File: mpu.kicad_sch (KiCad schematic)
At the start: 11 parts, among them IC1 MC6809E, SW1 RESET

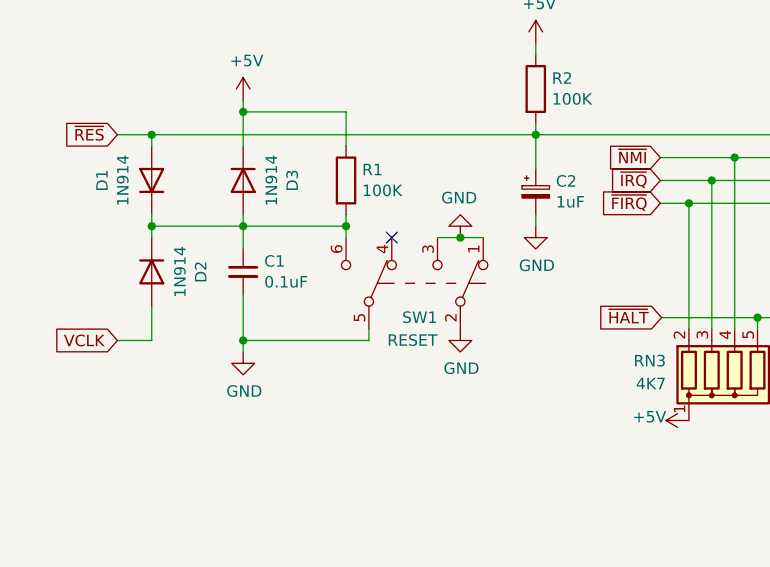
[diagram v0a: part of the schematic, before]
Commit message: rework to flex atx size
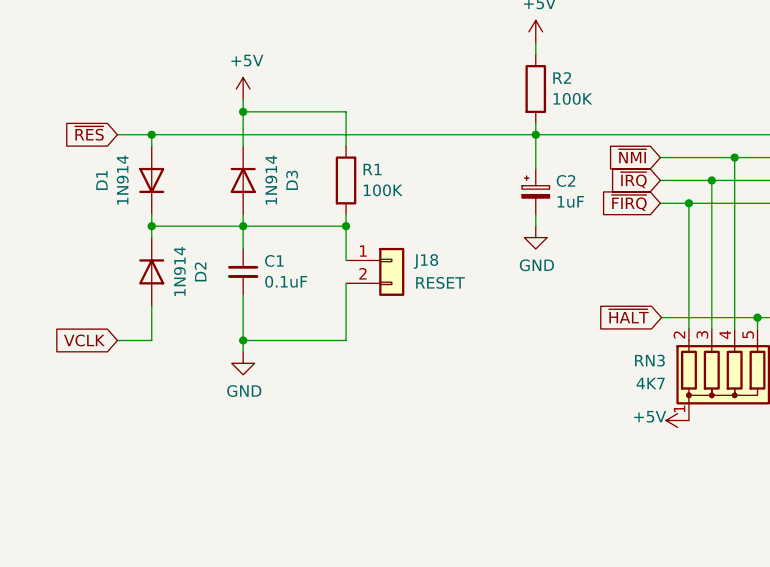
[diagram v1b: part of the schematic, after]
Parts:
- removed SW1: RESET, Dragon:Button_AlpsAlpine_SPUN190900, symbol Switch:SW_Push_DPDT
- added J18: RESET, Connector_PinHeader_2.54mm:PinHeader_1x02_P2.54mm_Vertical, symbol Connector_Generic:Conn_01x02
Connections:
- net GND: now also J18.2 (Pin_2)
- net at C1.1, D1.1 (K), D2.1 (K)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: now also J18.1 (Pin_1)
- no-connect marks 1 -> 0
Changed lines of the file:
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@@
-	)
-	(junction
-		(at 130.81 99.06)
-		(diameter 0)
-		(color 0 0 0 0)
 	)
 	(junction
@@
 		(color 0 0 0 0)
 	)
-	(no_connect
-		(at 123.19 99.06)
-	)
 	(bus_entry
 		(at 166.37 74.93)
@@
 	(wire
 		(pts
-			(xy 120.65 109.22) (xy 120.65 110.49)
-		)
-		(stroke
-			(width 0)
-			(type default)
-		)
-	)
-	(wire
-		(pts
 			(xy 96.52 97.79) (xy 96.52 99.06)
 		)
@@
 		)
 	)
-	(wire
-		(pts
-			(xy 130.81 99.06) (xy 133.35 99.06)
-		)
-		(stroke
-			(width 0)
-			(type default)
-		)
-	)
 	(bus
 		(pts
@@
 	(wire
 		(pts
-			(xy 128.27 99.06) (xy 130.81 99.06)
-		)
-		(stroke
-			(width 0)
-			(type default)
-		)
-	)
-	(wire
-		(pts
 			(xy 139.192 87.63) (xy 139.192 91.44)
 		)
@@
 	(wire
 		(pts
+			(xy 118.11 104.14) (xy 118.11 110.49)
+		)
+		(stroke
+			(width 0)
+			(type default)
+		)
+	)
+	(wire
+		(pts
 			(xy 200.66 64.77) (xy 196.85 64.77)
 		)
@@
 	(wire
 		(pts
+			(xy 118.11 110.49) (xy 106.68 110.49)
+		)
+		(stroke
+			(width 0)
+			(type default)
+		)
+	)
+	(wire
+		(pts
 			(xy 156.21 95.25) (xy 171.45 95.25)
 		)
@@
 	(wire
 		(pts
-			(xy 118.11 97.79) (xy 118.11 99.06)
-		)
-		(stroke
-			(width 0)
-			(type default)
-		)
-	)
-	(wire
-		(pts
 			(xy 200.66 77.47) (xy 196.85 77.47)
 		)
@@
 		)
 	)
+	(wire
+		(pts
+			(xy 118.11 97.79) (xy 118.11 101.6)
+		)
+		(stroke
+			(width 0)
+			(type default)
+		)
+	)
 	(bus
 		(pts
@@
 		(pts
 			(xy 203.2 64.77) (xy 203.2 62.23)
-		)
-		(stroke
-			(width 0)
-			(type default)
-		)
-	)
-	(wire
-		(pts
-			(xy 120.65 110.49) (xy 106.68 110.49)
 		)
 		(stroke
@@
 			)
 			(justify left)
-		)
-	)
-	(symbol
-		(lib_id "power:GND")
-		(at 130.81 99.06 180)
-		(unit 1)
-		(exclude_from_sim no)
-		(in_bom yes)
-		(on_board yes)
-		(dnp no)
-		(property "Reference" "#PWR0135"
-			(at 130.81 92.71 0)
-			(effects
-				(font
-					(size 1.27 1.27)
-				)
-				(hide yes)
-			)
-		)
-		(property "Value" "GND"
-			(at 130.683 94.6658 0)
-			(effects
-				(font
-					(size 1.27 1.27)
-				)
-			)
-		)
-		(property "Footprint" ""
-			(at 130.81 99.06 0)
-			(effects
-				(font
-					(size 1.27 1.27)
-				)
-				(hide yes)
-			)
-		)
-		(property "Datasheet" ""
-			(at 130.81 99.06 0)
-			(effects
-				(font
-					(size 1.27 1.27)
-				)
-				(hide yes)
-			)
-		)
-		(property "Description" ""
-			(at 130.81 99.06 0)
-			(effects
-				(font
-					(size 1.27 1.27)
-				)
-				(hide yes)
-			)
-		)
-		(pin "1"
-		)
-		(instances
-			(project "DragonRevX4Plus"
-				(path "/280624a6-9139-42c2-8c41-e9b53b8715d2/dfedbe1d-4fb5-427e-80c5-e29061a6defc"
-					(reference "#PWR0135")
-					(unit 1)
-				)
-			)
 		)
 	)
@@
 	)
 	(symbol
-		(lib_id "power:GND")
-		(at 130.81 109.22 0)
-		(unit 1)
-		(exclude_from_sim no)
-		(in_bom yes)
-		(on_board yes)
-		(dnp no)
-		(property "Reference" "#PWR064"
-			(at 130.81 115.57 0)
-			(effects
-				(font
-					(size 1.27 1.27)
-				)
-				(hide yes)
-			)
-		)
-		(property "Value" "GND"
-			(at 130.937 113.6142 0)
-			(effects
-				(font
-					(size 1.27 1.27)
-				)
-			)
-		)
-		(property "Footprint" ""
-			(at 130.81 109.22 0)
-			(effects
-				(font
-					(size 1.27 1.27)
-				)
-				(hide yes)
-			)
-		)
-		(property "Datasheet" ""
-			(at 130.81 109.22 0)
-			(effects
-				(font
-					(size 1.27 1.27)
-				)
-				(hide yes)
-			)
-		)
-		(property "Description" ""
-			(at 130.81 109.22 0)
-			(effects
-				(font
-					(size 1.27 1.27)
-				)
-				(hide yes)
-			)
-		)
-		(pin "1"
-		)
-		(instances
-			(project "DragonRevX4Plus"
-				(path "/280624a6-9139-42c2-8c41-e9b53b8715d2/dfedbe1d-4fb5-427e-80c5-e29061a6defc"
-					(reference "#PWR064")
-					(unit 1)
-				)
-			)
-		)
-	)
-	(symbol
 		(lib_id "Diode:1N914")
 		(at 106.68 92.71 270)
@@
 				(path "/280624a6-9139-42c2-8c41-e9b53b8715d2/dfedbe1d-4fb5-427e-80c5-e29061a6defc"
 					(reference "#PWR06")
+					(unit 1)
+				)
+			)
+		)
+	)
+	(symbol
+		(lib_id "Connector_Generic:Conn_01x02")
+		(at 123.19 101.6 0)
+		(unit 1)
+		(exclude_from_sim no)
+		(in_bom yes)
+		(on_board yes)
+		(dnp no)
+		(fields_autoplaced yes)
+		(property "Reference" "J18"
+			(at 125.73 101.5999 0)
+			(effects
+				(font
+					(size 1.27 1.27)
+				)
+				(justify left)
+			)
+		)
+		(property "Value" "RESET"
+			(at 125.73 104.1399 0)
+			(effects
+				(font
+					(size 1.27 1.27)
+				)
+				(justify left)
+			)
+		)
+		(property "Footprint" "Connector_PinHeader_2.54mm:PinHeader_1x02_P2.54mm_Vertical"
+			(at 123.19 101.6 0)
+			(effects
+				(font
+					(size 1.27 1.27)
+				)
+				(hide yes)
+			)
+		)
+		(property "Datasheet" "~"
+			(at 123.19 101.6 0)
+			(effects
+				(font
+					(size 1.27 1.27)
+				)
+				(hide yes)
+			)
+		)
+		(property "Description" "Generic connector, single row, 01x02, script generated (kicad-library-utils/schlib/autogen/connector/)"
+			(at 123.19 101.6 0)
+			(effects
+				(font
+					(size 1.27 1.27)
+				)
+				(hide yes)
+			)
+		)
+		(pin "2"
+		)
+		(pin "1"
+		)
+		(instances
+			(project "DragonRevX4Plus"
+				(path "/280624a6-9139-42c2-8c41-e9b53b8715d2/dfedbe1d-4fb5-427e-80c5-e29061a6defc"
+					(reference "J18")
 					(unit 1)
 				)
@@
 					(unit 1)
 				)
-			)
-		)
-	)
-	(symbol
-		(lib_id "Switch:SW_Push_DPDT")
-		(at 125.73 104.14 270)
-		(mirror x)
-		(unit 1)
-		(exclude_from_sim no)
-		(in_bom yes)
-		(on_board yes)
-		(dnp no)
-		(property "Reference" "SW1"
-			(at 128.27 107.95 90)
-			(effects
-				(font
-					(size 1.27 1.27)
-				)
-				(justify right)
-			)
-		)
-		(property "Value" "RESET"
-			(at 128.27 110.49 90)
-			(effects
-				(font
-					(size 1.27 1.27)
-				)
-				(justify right)
-			)
-		)
-		(property "Footprint" "Dragon:Button_AlpsAlpine_SPUN190900"
-			(at 130.81 104.14 0)
-			(effects
-				(font
-					(size 1.27 1.27)
-				)
-				(hide yes)
-			)
-		)
-		(property "Datasheet" "https://www.ckswitches.com/media/1402/fpush.pdf"
-			(at 130.81 104.14 0)
-			(effects
-				(font
-					(size 1.27 1.27)
-				)
-				(hide yes)
-			)
-		)
-		(property "Description" ""
-			(at 125.73 104.14 0)
-			(effects
-				(font
-					(size 1.27 1.27)
-				)
-				(hide yes)
-			)
-		)
-		(property "DigiKey" "401-1225-ND"
-			(at 125.73 104.14 90)
-			(effects
-				(font
-					(size 1.27 1.27)
-				)
-				(hide yes)
-			)
-		)
-		(pin "1"
-		)
-		(pin "2"
-		)
-		(pin "3"
-		)
-		(pin "4"
-		)
-		(pin "5"
-		)
-		(pin "6"
-		)
-		(instances
-			(project "DragonRevX4Plus"
-				(path "/280624a6-9139-42c2-8c41-e9b53b8715d2/dfedbe1d-4fb5-427e-80c5-e29061a6defc"
-					(reference "SW1")
-					(unit 1)
-				)

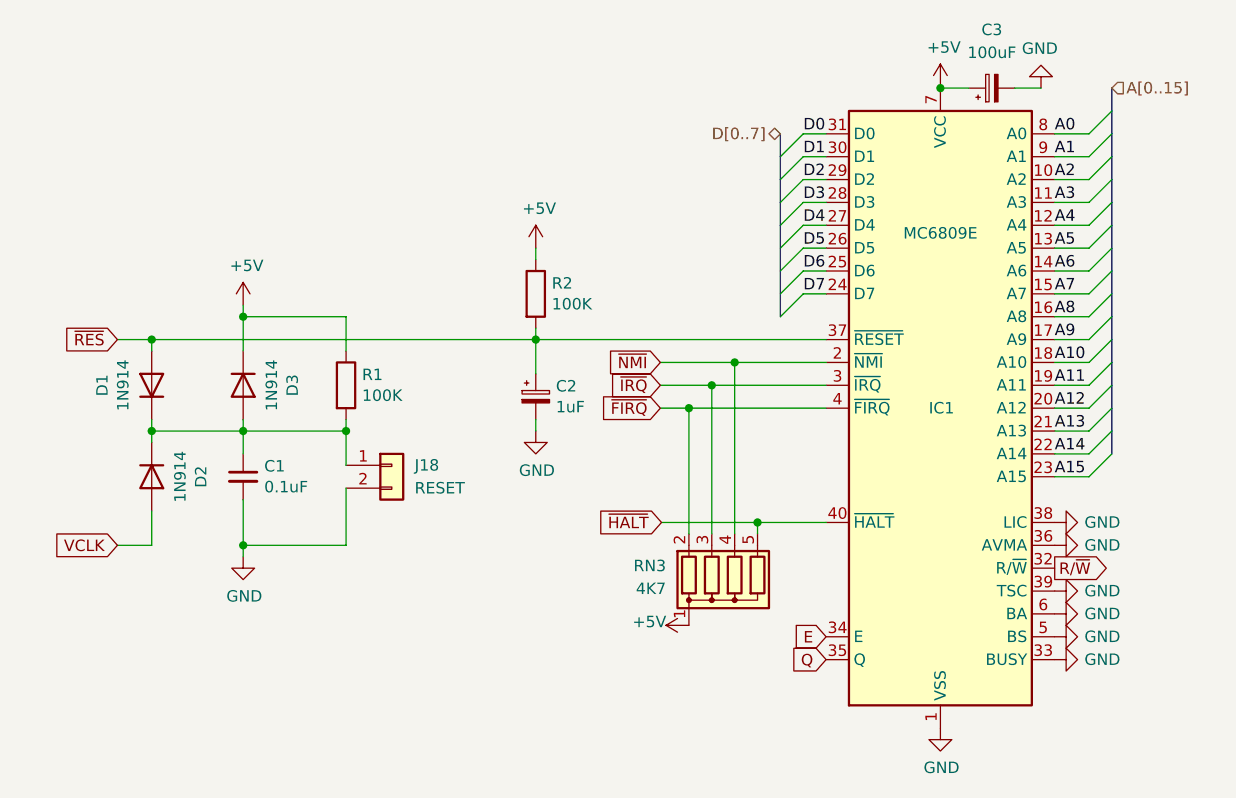
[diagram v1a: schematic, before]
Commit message: route data bus to sam
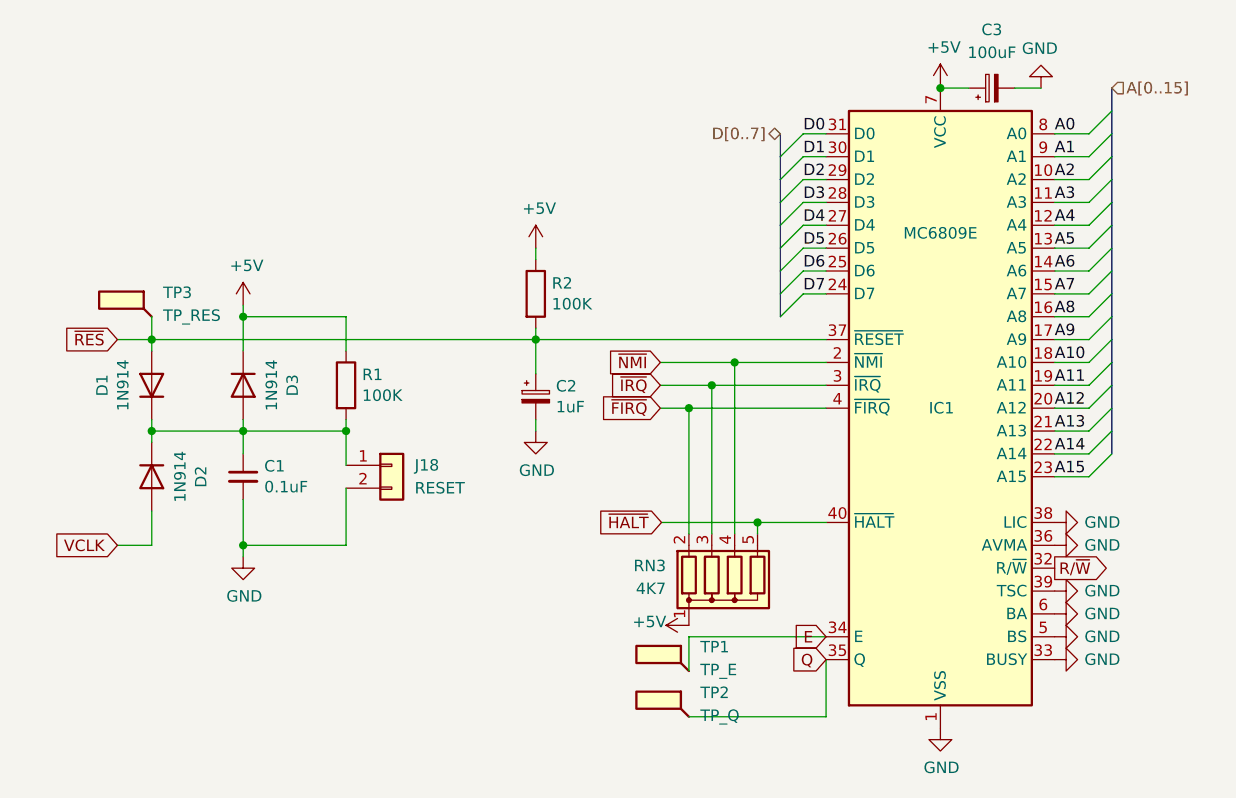
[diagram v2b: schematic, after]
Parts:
- added TP1: TP_E, TestPoint:TestPoint_Loop_D1.80mm_Drill1.0mm_Beaded, symbol Connector:TestPoint_Flag
- added TP2: TP_Q, TestPoint:TestPoint_Loop_D1.80mm_Drill1.0mm_Beaded, symbol Connector:TestPoint_Flag
- added TP3: TP_RES, TestPoint:TestPoint_Loop_D1.80mm_Drill1.0mm_Beaded, symbol Connector:TestPoint_Flag
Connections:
- net E: now also TP1.1
- net Q: now also TP2.1
- net ~{RES}: now also TP3.1
